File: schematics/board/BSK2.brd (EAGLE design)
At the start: 82 x 100 mm, 43 parts

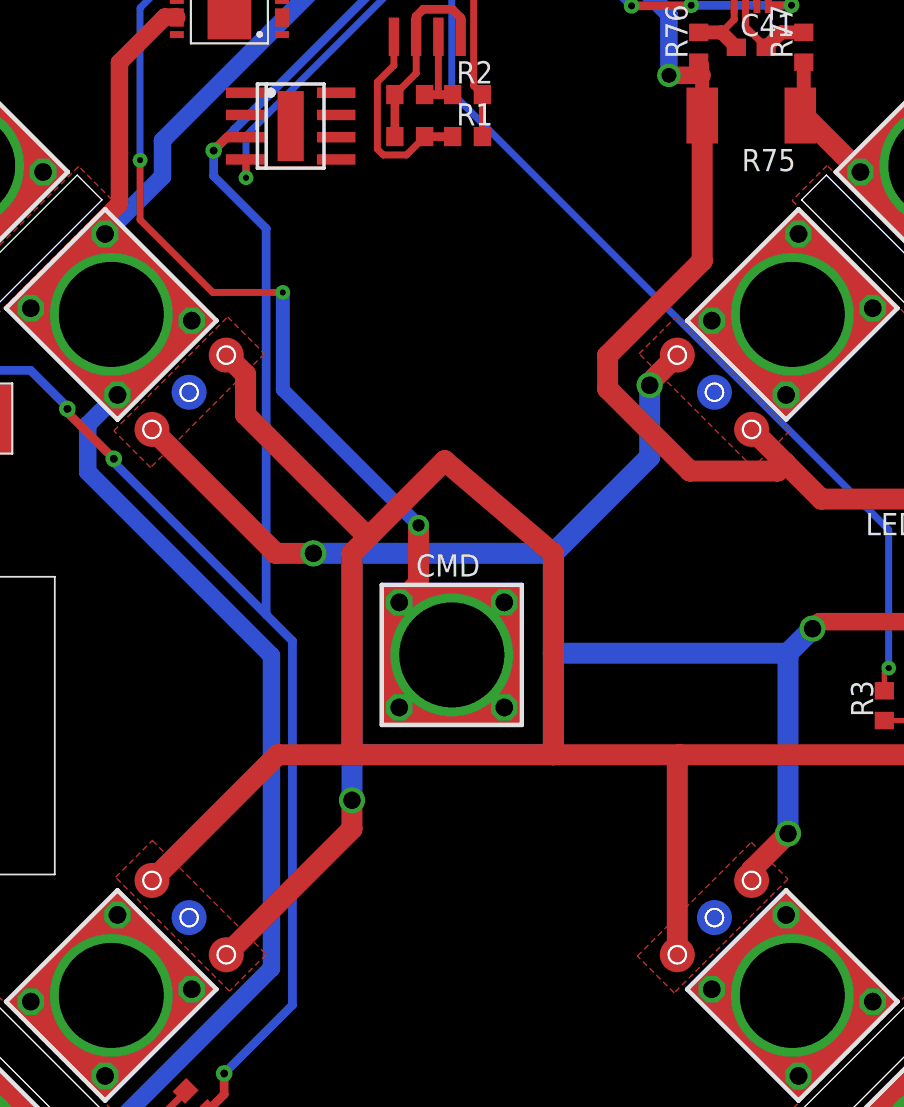
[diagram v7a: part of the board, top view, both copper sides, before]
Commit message: Изменены площадки для сплавов Розе
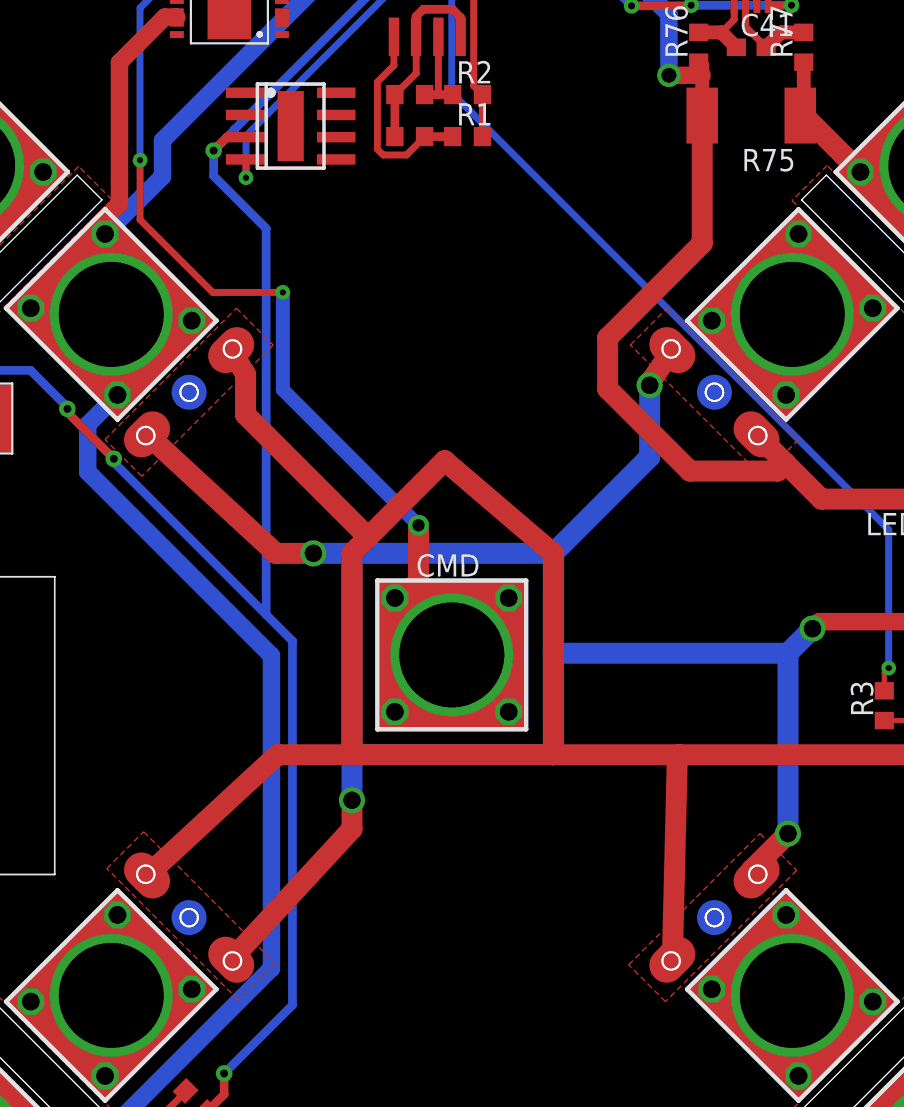
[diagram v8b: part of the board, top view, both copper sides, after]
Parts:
- U$15, U$16, U$6, U$7: value GRAFITGRAFIT3_1 -> GRAFITGRAFIT4_2; device CanCubeSat:GRAFIT3_1 -> CanCubeSat:GRAFIT4_2
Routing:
- net B2-CMD: track 73.6 -> 75.1 mm
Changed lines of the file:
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@@
 <attribute name="VALUE" x="67.865" y="44.695" size="1.27" layer="27"/>
 </element>
-<element name="U$6" library="CanCubeSat" package="GRAFIT3_1" value="GRAFITGRAFIT3_1" x="56" y="65" smashed="yes" rot="R45"/>
-<element name="U$7" library="CanCubeSat" package="GRAFIT3_1" value="GRAFITGRAFIT3_1" x="26" y="65" smashed="yes" rot="R135"/>
-<element name="U$15" library="CanCubeSat" package="GRAFIT3_1" value="GRAFITGRAFIT3_1" x="56" y="35" smashed="yes" rot="R315"/>
-<element name="U$16" library="CanCubeSat" package="GRAFIT3_1" value="GRAFITGRAFIT3_1" x="26" y="35" smashed="yes" rot="R225"/>
+<element name="U$6" library="CanCubeSat" package="GRAFIT4_2" value="GRAFITGRAFIT4_2" x="56" y="65" smashed="yes" rot="R45"/>
+<element name="U$7" library="CanCubeSat" package="GRAFIT4_2" value="GRAFITGRAFIT4_2" x="26" y="65" smashed="yes" rot="R135"/>
+<element name="U$15" library="CanCubeSat" package="GRAFIT4_2" value="GRAFITGRAFIT4_2" x="56" y="35" smashed="yes" rot="R315"/>
+<element name="U$16" library="CanCubeSat" package="GRAFIT4_2" value="GRAFITGRAFIT4_2" x="26" y="35" smashed="yes" rot="R225"/>
 <element name="CMD" library="CanCubeSat" package="KCONNECT_QUAD" value="KCONNECTQUAD" x="41" y="50" smashed="yes">
 <attribute name="NAME" x="38.96" y="54.475" size="1.27" layer="25" ratio="10"/>
@@
 <contactref element="U$57" pad="8"/>
 <polygon width="0.15" layer="1" pour="cutout" thermals="no">
-<vertex x="21.7" y="62.8"/>
-<vertex x="28.2" y="69.3"/>
-<vertex x="30.3" y="67.2"/>
-<vertex x="23.8" y="60.7"/>
+<vertex x="21.2" y="62.3"/>
+<vertex x="28.7" y="69.8"/>
+<vertex x="30.8" y="67.7"/>
+<vertex x="23.3" y="60.2"/>
 </polygon>
 <contactref element="BKU" pad="9"/>
@@
 <contactref element="CMD" pad="3"/>
 <contactref element="CMD" pad="P$1"/>
-<wire x1="41" y1="50" x2="38" y2="47" width="0.4" layer="1"/>
-<wire x1="41" y1="50" x2="38" y2="53" width="0.4" layer="1"/>
-<wire x1="41" y1="50" x2="44" y2="47" width="0.4" layer="1"/>
-<wire x1="41" y1="50" x2="44" y2="53" width="0.4" layer="1"/>
+<wire x1="41" y1="50" x2="37.75" y2="46.75" width="0.4" layer="1"/>
+<wire x1="41" y1="50" x2="37.75" y2="53.25" width="0.4" layer="1"/>
+<wire x1="41" y1="50" x2="44.25" y2="46.75" width="0.4" layer="1"/>
+<wire x1="41" y1="50" x2="44.25" y2="53.25" width="0.4" layer="1"/>
 <wire x1="26.92" y1="98.75" x2="26.9" y2="98.73" width="0.4" layer="16"/>
 <wire x1="26.9" y1="98.73" x2="26.9" y2="90.65" width="0.4" layer="16"/>
@@
 <wire x1="31.35" y1="65.15" x2="31.35" y2="70.7" width="0.8" layer="16"/>
 <wire x1="39.1" y1="57.4" x2="39.1" y2="54.1" width="1.2" layer="1"/>
-<wire x1="39.1" y1="54.1" x2="38" y2="53" width="1.2" layer="1"/>
+<wire x1="39.1" y1="54.1" x2="37.75" y2="53.25" width="1.2" layer="1"/>
 </signal>
 <signal name="BUS+">
@@
 <contactref element="R75" pad="2"/>
 <contactref element="R76" pad="1"/>
-<wire x1="28.12131875" y1="67.12131875" x2="29.22131875" y2="66.02131875" width="1.2" layer="1"/>
+<wire x1="28.4041625" y1="67.4041625" x2="29.22131875" y2="66.02131875" width="1.2" layer="1"/>
 <wire x1="29.22131875" y1="66.02131875" x2="29.22131875" y2="63.72131875" width="1.2" layer="1"/>
 <wire x1="29.22131875" y1="63.72131875" x2="36.22131875" y2="56.72131875" width="1.2" layer="1"/>
-<wire x1="58.12131875" y1="62.878678125" x2="60.05" y2="60.949996875" width="1.2" layer="1"/>
+<wire x1="58.4041625" y1="62.595834375" x2="60.05" y2="60.949996875" width="1.2" layer="1"/>
 <wire x1="60.05" y1="60.949996875" x2="62.099996875" y2="58.9" width="1.2" layer="1"/>
 <wire x1="68" y1="58.9" x2="70.1" y2="56.8" width="1.2" layer="1"/>
 <wire x1="62.099996875" y1="58.9" x2="68" y2="58.9" width="1.2" layer="1"/>
-<wire x1="53.878678125" y1="32.878678125" x2="53.878678125" y2="44.178678125" width="1.2" layer="1"/>
+<wire x1="53.595834375" y1="32.595834375" x2="53.878678125" y2="44.178678125" width="1.2" layer="1"/>
 <wire x1="53.878678125" y1="44.178678125" x2="54" y2="44.3" width="1.2" layer="1"/>
-<wire x1="23.878678125" y1="37.12131875" x2="31.057359375" y2="44.3" width="1.2" layer="1"/>
+<wire x1="23.595834375" y1="37.4041625" x2="31.057359375" y2="44.3" width="1.2" layer="1"/>
 <wire x1="31.057359375" y1="44.3" x2="35.3" y2="44.3" width="1.2" layer="1"/>
 <wire x1="36.22131875" y1="56.72131875" x2="40.592175" y2="61.092175" width="1.2" layer="1"/>
@@
 <wire x1="42.8" y1="97.188" x2="53.4" y2="86.588" width="1" layer="16"/>
 <wire x1="53.4" y1="86.588" x2="53.4" y2="83.1" width="1" layer="16"/>
-<wire x1="55.3" y1="80.8" x2="55.3" y2="72.5" width="1.2" layer="1"/>
-<wire x1="49.9" y1="67.1" x2="49.9" y2="65.2" width="1.2" layer="1"/>
-<wire x1="55.3" y1="72.5" x2="49.9" y2="67.1" width="1.2" layer="1"/>
+<wire x1="55.3" y1="80.8" x2="55.3" y2="73.5" width="1.2" layer="1"/>
+<wire x1="49.9" y1="68.1" x2="49.9" y2="65.2" width="1.2" layer="1"/>
+<wire x1="55.3" y1="73.5" x2="49.9" y2="68.1" width="1.2" layer="1"/>
 <wire x1="60.05" y1="60.949996875" x2="59.600003125" y2="60.5" width="1.2" layer="1"/>
 <wire x1="59.600003125" y1="60.5" x2="54.6" y2="60.5" width="1.2" layer="1"/>
@@
 <wire x1="46.8" y1="44.3" x2="46.8" y2="50.1" width="1.2" layer="16"/>
 <wire x1="46.8" y1="50.1" x2="46.8" y2="55.8" width="1.2" layer="16"/>
-<wire x1="58.12131875" y1="37.12131875" x2="58.12131875" y2="37.72131875" width="1.2" layer="1"/>
+<wire x1="58.4041625" y1="37.4041625" x2="58.12131875" y2="37.72131875" width="1.2" layer="1"/>
 <wire x1="58.12131875" y1="37.72131875" x2="60.2" y2="39.8" width="1.2" layer="1"/>
 <wire x1="60.2" y1="39.8" x2="60.2" y2="50.1" width="1.2" layer="16"/>
@@
 <wire x1="46.8" y1="50.1" x2="60.2" y2="50.1" width="1.2" layer="16"/>
 <wire x1="35.3" y1="55.8" x2="46.8" y2="55.8" width="1.2" layer="16"/>
-<wire x1="28.12131875" y1="32.878678125" x2="35.3" y2="40.057359375" width="1.2" layer="1"/>
+<wire x1="28.4041625" y1="32.595834375" x2="35.3" y2="40.057359375" width="1.2" layer="1"/>
 <wire x1="35.3" y1="40.057359375" x2="35.3" y2="41.7" width="1.2" layer="1"/>
 <via x="35.3" y="41.7" extent="1-16" drill="1"/>
 <wire x1="35.3" y1="41.7" x2="35.3" y2="44.3" width="1.2" layer="16"/>
-<wire x1="23.878678125" y1="62.878678125" x2="30.95735625" y2="55.8" width="1.2" layer="1"/>
+<wire x1="23.595834375" y1="62.595834375" x2="30.95735625" y2="55.8" width="1.2" layer="1"/>
 <wire x1="30.95735625" y1="55.8" x2="33.1" y2="55.8" width="1.2" layer="1"/>
 <via x="33.1" y="55.8" extent="1-16" drill="1"/>
@@
 <wire x1="52.3" y1="61.3" x2="52.3" y2="65.4" width="1.2" layer="16"/>
 <via x="52.3" y="65.4" extent="1-16" drill="1"/>
-<wire x1="53.878678125" y1="67.12131875" x2="52.3" y2="65.542640625" width="1.2" layer="1"/>
+<wire x1="53.595834375" y1="67.4041625" x2="52.3" y2="65.542640625" width="1.2" layer="1"/>
 <wire x1="52.3" y1="65.542640625" x2="52.3" y2="65.4" width="1.2" layer="1"/>
 </signal>
@@
 <signal name="GND1">
 <polygon width="0.15" layer="1" pour="cutout" thermals="no">
-<vertex x="58.2" y="60.7"/>
-<vertex x="51.7" y="67.2"/>
-<vertex x="53.8" y="69.3"/>
-<vertex x="60.3" y="62.8"/>
+<vertex x="58.7" y="60.2"/>
+<vertex x="51.2" y="67.7"/>
+<vertex x="53.3" y="69.8"/>
+<vertex x="60.8" y="62.3"/>
 </polygon>
 </signal>
 <signal name="GND2">
 <polygon width="0.15" layer="1" pour="cutout" thermals="no">
-<vertex x="51.6" y="32.8"/>
-<vertex x="58.1" y="39.3"/>
-<vertex x="60.2" y="37.2"/>
-<vertex x="53.7" y="30.7"/>
+<vertex x="51.1" y="32.3"/>
+<vertex x="58.6" y="39.8"/>
+<vertex x="60.7" y="37.7"/>
+<vertex x="53.2" y="30.2"/>
 </polygon>
 </signal>
 <signal name="GND3">
 <polygon width="0.15" layer="1" pour="cutout" thermals="no">
-<vertex x="28.3" y="30.8"/>
-<vertex x="21.8" y="37.3"/>
-<vertex x="23.9" y="39.4"/>
-<vertex x="30.4" y="32.9"/>
-</polygon>
-</signal>
+<vertex x="28.8" y="30.3"/>
+<vertex x="21.3" y="37.8"/>
+<vertex x="23.4" y="39.9"/>
+<vertex x="30.9" y="32.4"/>
+</polygon>
+</signal>
